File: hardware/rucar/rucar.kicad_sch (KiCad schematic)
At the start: 30 parts

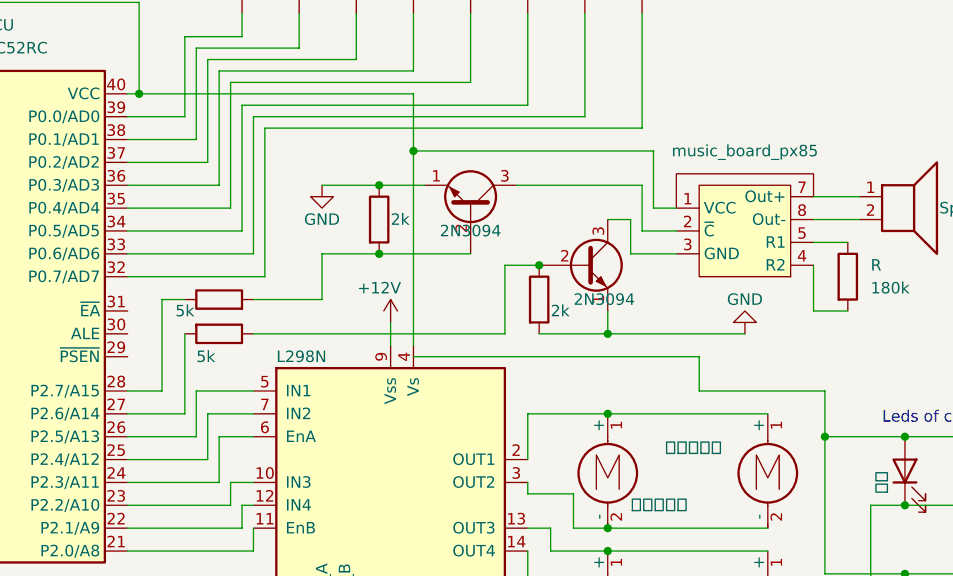
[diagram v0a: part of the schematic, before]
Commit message: change switch to pwm module.
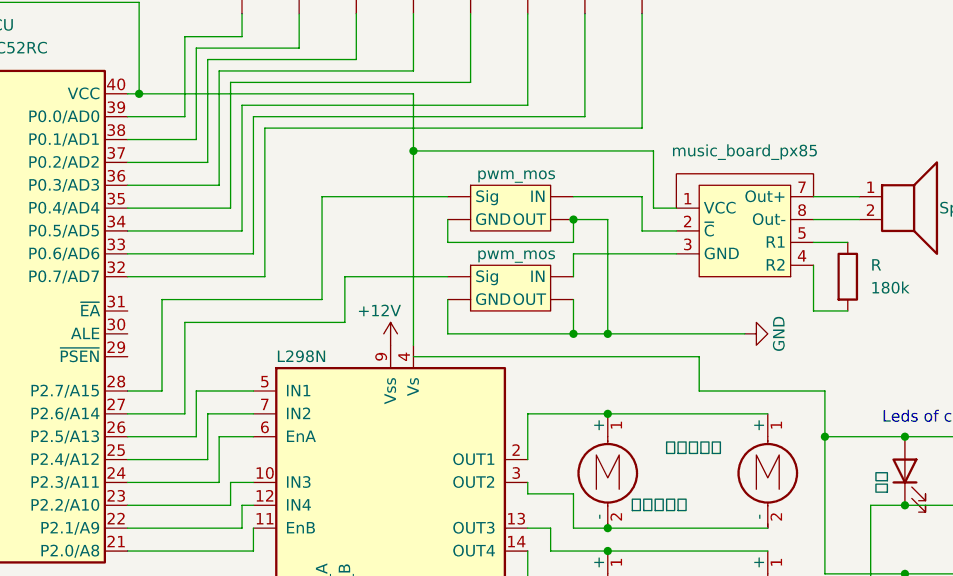
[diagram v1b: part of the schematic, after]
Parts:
- removed Q: 2N3094, Package_TO_SOT_THT:TO-92_Inline, symbol Transistor_BJT:2N3904
- removed Q?: 2N3094, Package_TO_SOT_THT:TO-39-3, symbol Transistor_BJT:2N2219
- removed R? (x2): 5k, symbol Device:R
- removed R? (x2): 2k, symbol Device:R
- added U? (x2): pwm_mos, symbol Power_Management:pwm_mos
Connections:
- net GND: now also U?. (Sig), U?. (Sig)
- net at MCU.27 (P2.6/A14): now also U?. (Sig)
- net at U?.2 (~{C}): now also U?. (Sig)
- net at U?.3 (GND): now also U?. (Sig)
- net at MCU.28 (P2.7/A15): now also U?. (Sig)

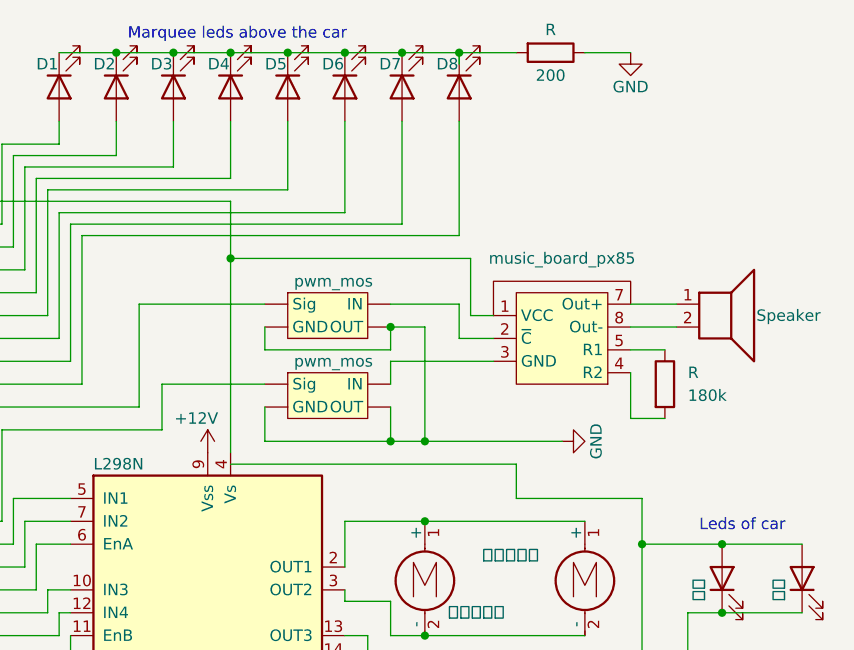
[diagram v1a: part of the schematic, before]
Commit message: change music board to flm038-sop8-body
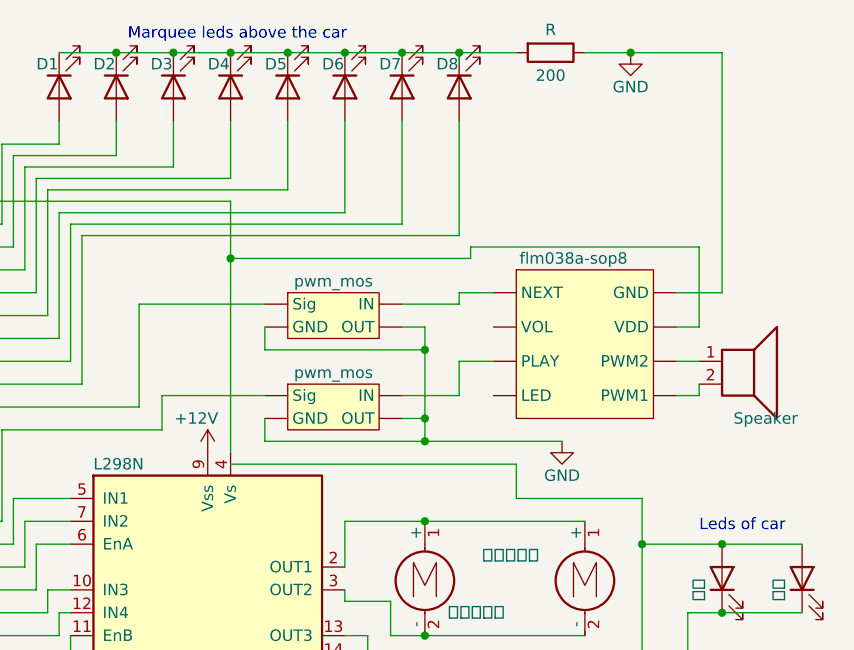
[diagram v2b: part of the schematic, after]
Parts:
- removed R: 180k, symbol Device:R
- removed U?: music_board_px85, symbol Audio:music_board_px85
- removed U? (x2): pwm_mos, symbol Power_Management:pwm_mos
- added U? (x2): pwm_mos, symbol Power_Management:pwm_mos
- added U?: flm038a-sop8, symbol Audio:flm038a-sop8
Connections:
- net GND: now also U?. (Sig), U?. (Sig), U?. (VOL)
- net at MCU.40 (VCC), U?.4 (Vs), U?.5 (VDD): now also U?. (VOL)
- net at LS?.1: now also U?. (VOL)
- net at LS?.2: now also U?. (VOL)
- net at MCU.27 (P2.6/A14): now also U?. (Sig)
- net at MCU.28 (P2.7/A15): now also U?. (Sig)
- new net: U?. (Sig), U?. (VOL) (x2)

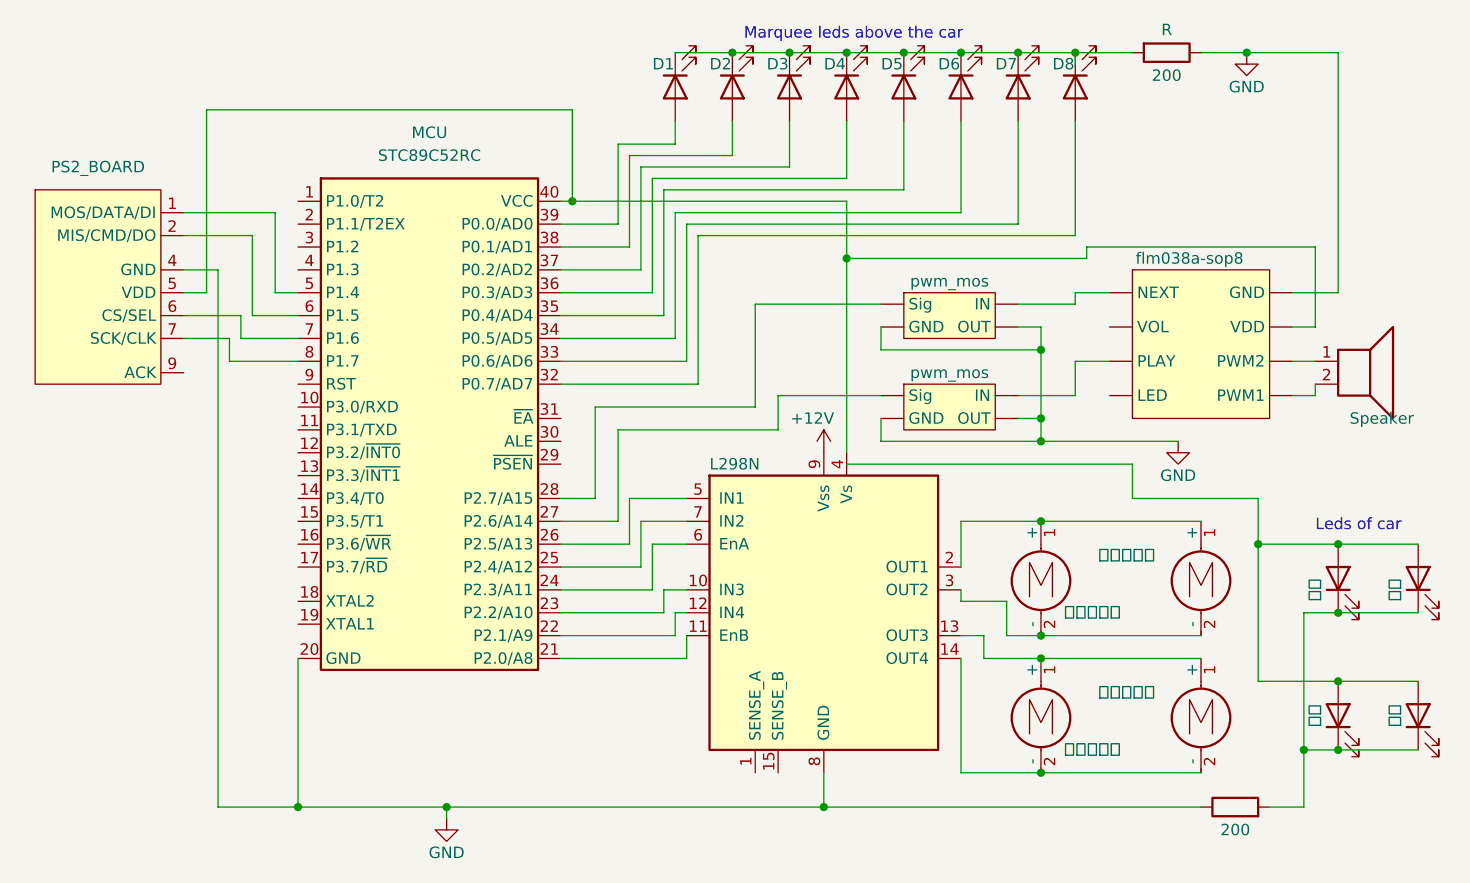
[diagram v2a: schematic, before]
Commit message: change led to control module.
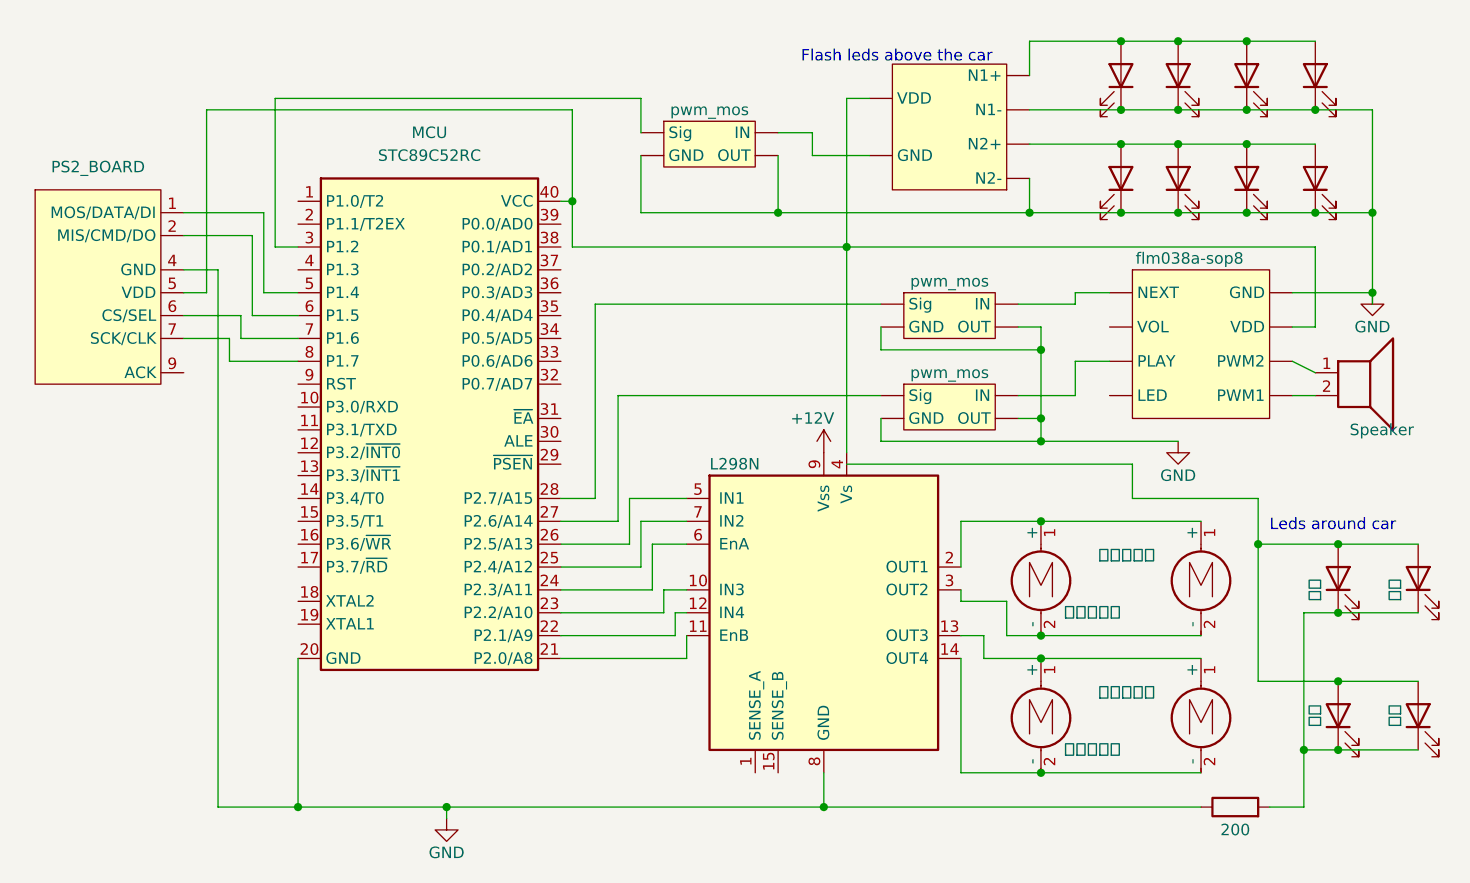
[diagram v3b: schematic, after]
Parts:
- removed D: D4, symbol Device:LED
- removed D: D8, symbol Device:LED
- removed D: D3, symbol Device:LED
- removed D: D7, symbol Device:LED
- removed D: D1, symbol Device:LED
- removed D: D2, symbol Device:LED
- removed D: D5, symbol Device:LED
- removed D: D6, symbol Device:LED
- removed R: 200, symbol Device:R
- added D? (x8): LED, symbol Device:LED
- added U?: pwm_mos, symbol Power_Management:pwm_mos
- added U?: self_define_led_driver, symbol Driver_LED:self_define_led_driver
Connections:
- net GND: now also D?.1 (K), D?.1 (K), D?.1 (K), D?.1 (K), D?.1 (K), D?.1 (K), D?.1 (K), D?.1 (K), U?. (Sig), U?. (VDD)
- net at MCU.3 (P1.2): now also U?. (Sig)
- net at MCU.40 (VCC), U?. (VOL), U?.4 (Vs)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: now also U?. (VDD)
- new net: D?.2 (A), D?.2 (A), D?.2 (A), D?.2 (A), U?. (VDD) (x2)
- new net: U?. (Sig), U?. (VOL) (x2)
- new net: U?. (Sig), U?. (VDD)
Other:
- note added: "Flash leds above the car"
- note added: "Leds around car"
- note removed: "Leds of car"
- note removed: "Marquee leds above the car"

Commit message: fix some description.
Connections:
- new net: U?. (Sig), U?. (VOL) (x2)
- new net: U?. (Sig), U?. (VDD)

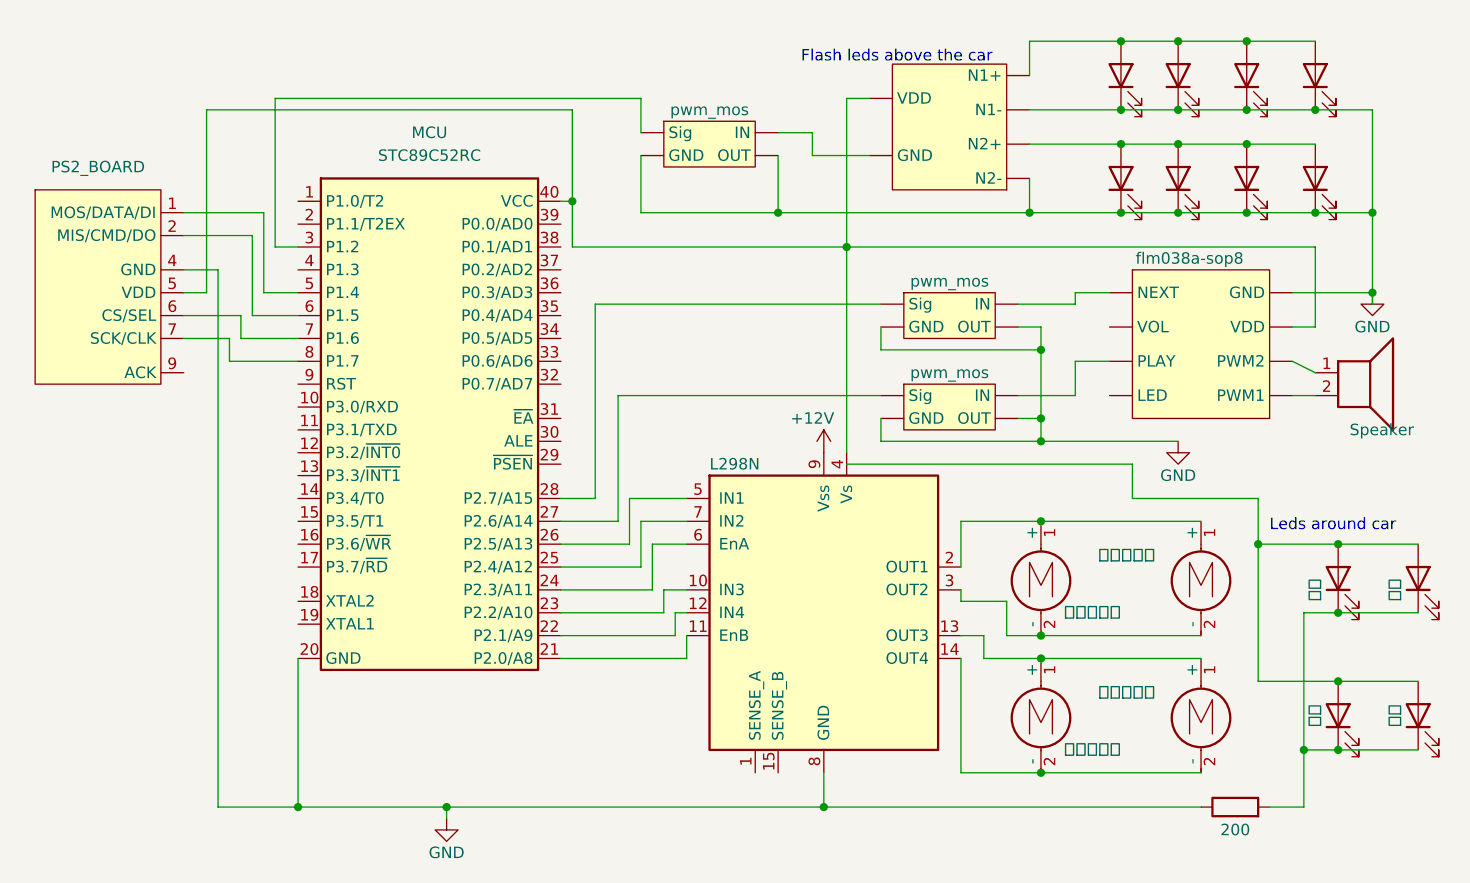
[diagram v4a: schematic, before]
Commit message: fix the pwm use method
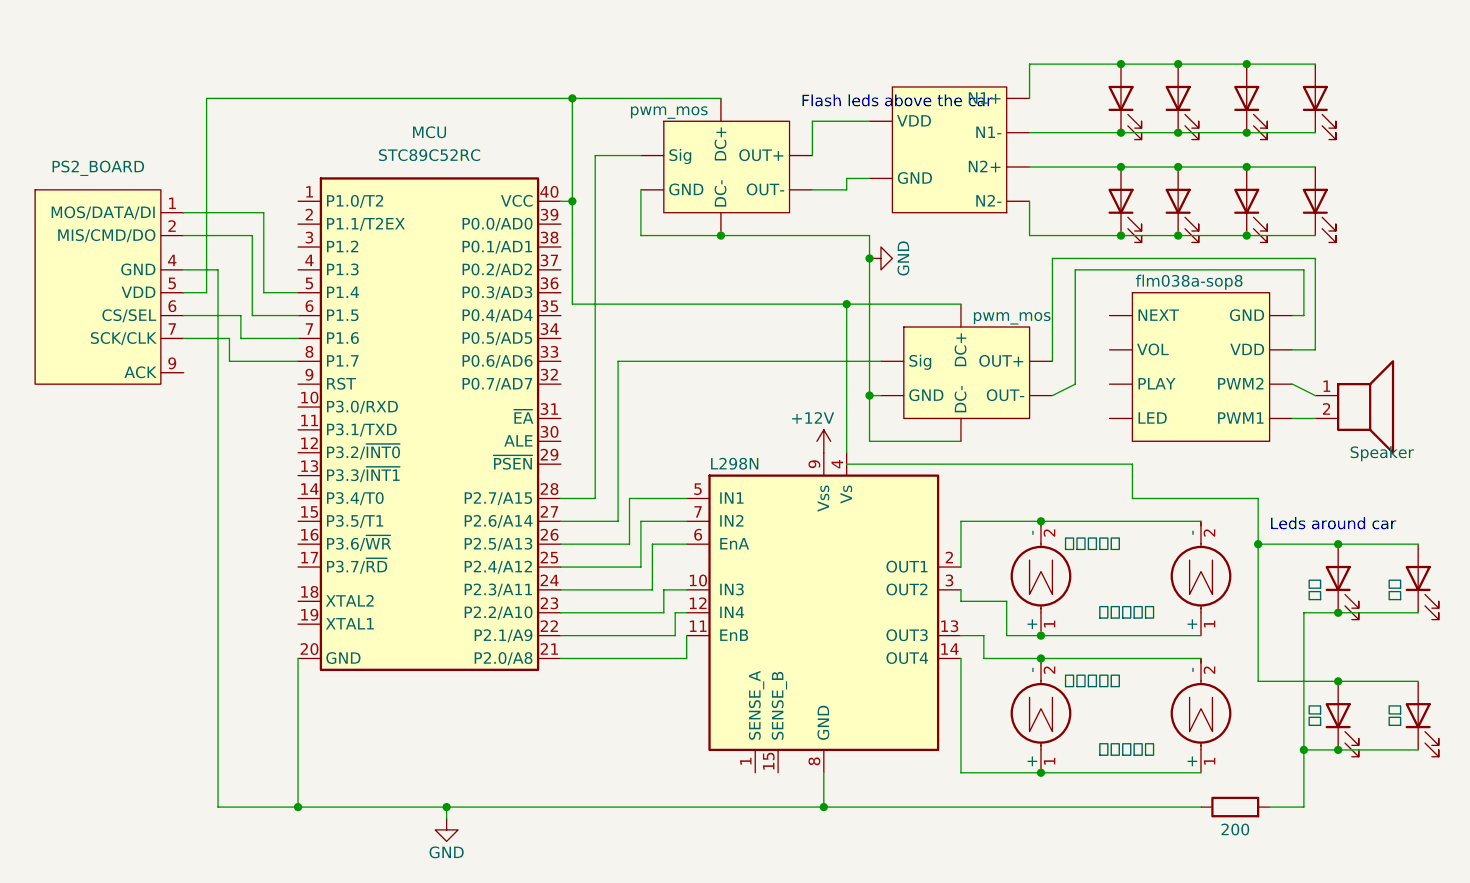
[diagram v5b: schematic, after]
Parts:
- removed U? (x3): pwm_mos, symbol Power_Management:pwm_mos
- added U? (x2): pwm_mos, symbol Power_Management:pwm_mos
- M?: value 右后轮电机 -> 左后轮电机
- M?: value 右前轮电机 -> 左前轮电机
- M?: value 左前轮电机 -> 右前轮电机
- M?: value 左后轮电机 -> 右后轮电机
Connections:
- net GND: now also U?. (Sig), U?. (Sig); no longer D?.1 (K), D?.1 (K), D?.1 (K), D?.1 (K), D?.1 (K), D?.1 (K), D?.1 (K), D?.1 (K), U?. (VDD), U?. (VOL)
- net at MCU.27 (P2.6/A14): now also U?. (Sig)
- net at MCU.28 (P2.7/A15): now also U?. (Sig)
- net at MCU.40 (VCC), U?.4 (Vs), U?.5 (VDD): now also U?. (Sig), U?. (Sig); no longer U?. (VDD), U?. (VOL)
- net at M?.1 (+), M?.1 (+): now also U?.14 (OUT4); no longer U?.13 (OUT3)
- net at M?.2 (-), M?.2 (-): now also U?.13 (OUT3); no longer U?.14 (OUT4)
- net at M?.1 (+), M?.1 (+): now also U?.3 (OUT2); no longer U?.2 (OUT1)
- net at M?.2 (-), M?.2 (-): now also U?.2 (OUT1); no longer U?.3 (OUT2)
- net at U?. (VOL): now also LS?.2
- new net: D?.1 (K), D?.1 (K), D?.1 (K), D?.1 (K), U?. (VDD) (x2)
- new net: U?. (Sig), U?. (VDD) (x2)
- new net: U?. (Sig), U?. (VOL) (x2)

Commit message: change gpio of motor driver.
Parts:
- M?: value 左后轮电机 -> 右后轮电机
- M?: value 左前轮电机 -> 右前轮电机
- M?: value 右前轮电机 -> 左前轮电机
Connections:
- net at U?. (VDD): now also D?.2 (A), D?.2 (A), D?.2 (A), D?.2 (A); no longer U?. (Sig)
- net at U?. (VOL): now also LS?.2; no longer U?. (Sig)
- new net: U?. (Sig), U?. (VDD) (x2)
- new net: U?. (Sig), U?. (VOL) (x2)
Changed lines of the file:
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@@
       (effects (font (size 1.27 1.27)) (justify left) hide)
     )
-    (property "Value" "左后轮电机" (id 1) (at 179.07 100.33 0)
+    (property "Value" "右后轮电机" (id 1) (at 179.07 100.33 0)
       (effects (font (size 1.27 1.27)) (justify left))
     )
@@
       (effects (font (size 1.27 1.27)) (justify left) hide)
     )
-    (property "Value" "左前轮电机" (id 1) (at 182.88 107.95 0)
+    (property "Value" "右前轮电机" (id 1) (at 182.88 107.95 0)
       (effects (font (size 1.27 1.27)) (justify left))
     )
@@
       (effects (font (size 1.27 1.27)) (justify left) hide)
     )
-    (property "Value" "右前轮电机" (id 1) (at 182.88 92.71 0)
+    (property "Value" "左前轮电机" (id 1) (at 182.88 92.71 0)
       (effects (font (size 1.27 1.27)) (justify left))
     )
@@
     )
     (path "/30289ba7-3bac-47ee-9847-37a985d5fd11"
-      (reference "M?") (unit 1) (value "左后轮电机") (footprint "")
+      (reference "M?") (unit 1) (value "右后轮电机") (footprint "")
     )
     (path "/4042b25f-2c64-4a49-a101-38d939f98ee4"
+      (reference "M?") (unit 1) (value "右前轮电机") (footprint "")
+    )
+    (path "/74e3e3a9-d10f-4405-bf6b-20df510cc5f7"
       (reference "M?") (unit 1) (value "左前轮电机") (footprint "")
     )
-    (path "/74e3e3a9-d10f-4405-bf6b-20df510cc5f7"
-      (reference "M?") (unit 1) (value "右前轮电机") (footprint "")
-    )
     (path "/ce4d2b31-1cfb-49cf-ae5a-fb9edfcff7ff"
